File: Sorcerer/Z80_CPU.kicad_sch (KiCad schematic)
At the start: 8 parts, among them U1 74LS241, U3 Z80CPU

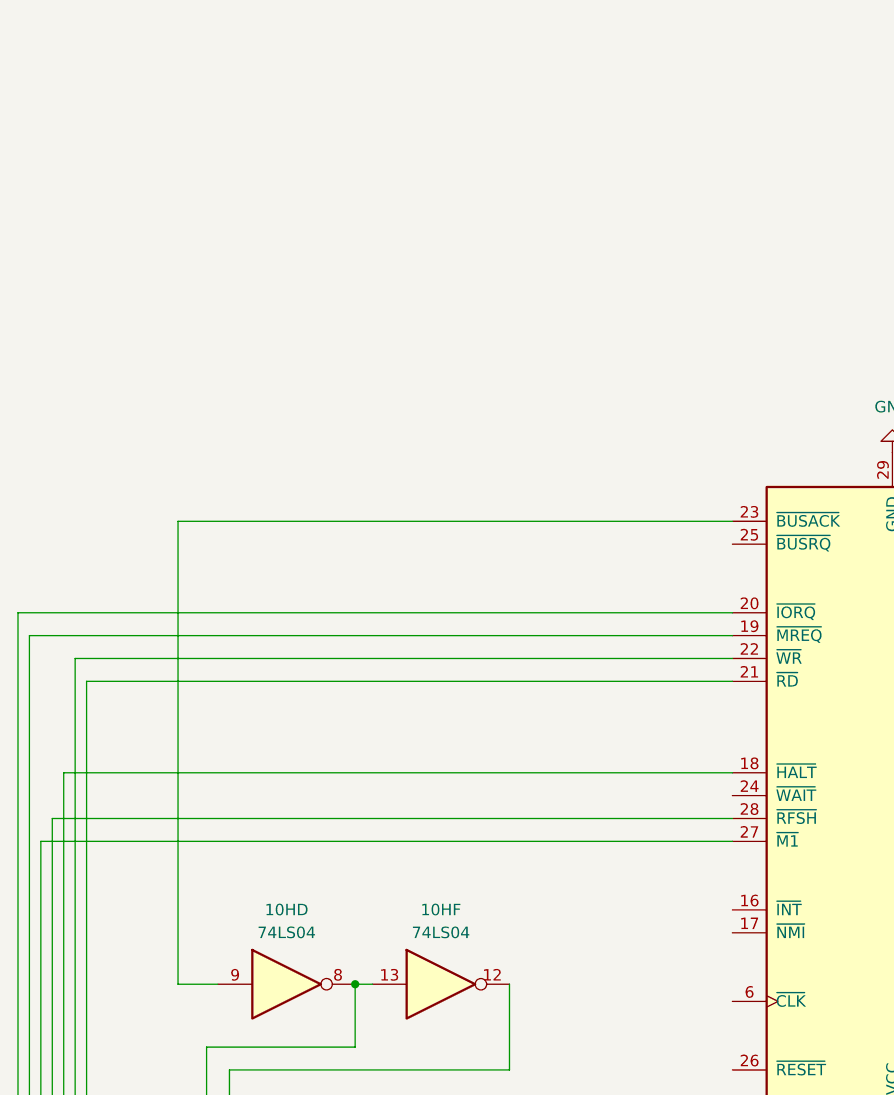
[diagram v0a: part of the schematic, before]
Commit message: More external symbols
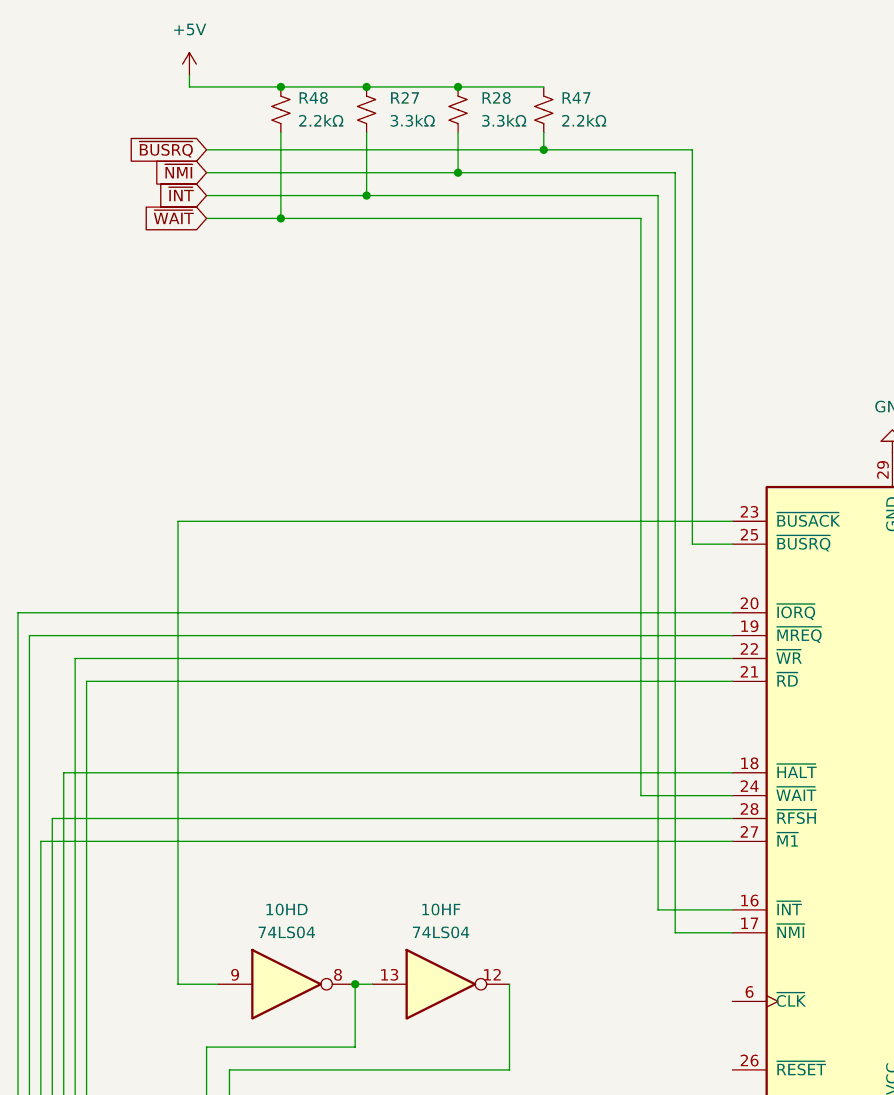
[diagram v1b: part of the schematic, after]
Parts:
- added R27, R28: 3.3kΩ, symbol Device:R_Small_US
- added R47, R48: 2.2kΩ, symbol Device:R_Small_US
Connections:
- net +5V: now also R27.1, R28.1, R47.1, R48.1
- net ~{INT}: now reaches U3.16 (~{INT})
- net ~{INT}: now also R27.2
- net ~{NMI}: now reaches U3.17 (~{NMI})
- net ~{NMI}: now also R28.2
- net ~{WAIT}: now reaches U3.24 (~{WAIT})
- net ~{WAIT}: now also R48.2
- net ~{BUSRQ}: now reaches U3.25 (~{BUSRQ})
- net ~{BUSRQ}: now also R47.2

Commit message: Clock generation
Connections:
- net ~{RESET}: now also U3.26 (~{RESET})
- net ~{BUSACK}: now reaches 10H.12, 6E.19 (OEb), 6F.19 (OEb), U1.19 (OEb)
- net Z80_Clock: now reaches U3.6 (~{CLK})
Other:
- added sheet Clock-Reset (Z80_Clock_Reset.kicad_sch)
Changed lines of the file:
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@@
 	)
 	(junction
+		(at 74.295 128.27)
+		(diameter 0)
+		(color 0 0 0 0)
+	)
+	(junction
 		(at 40.64 176.53)
 		(diameter 0)
@@
 	(wire
 		(pts
+			(xy 97.155 146.685) (xy 74.295 146.685)
+		)
+		(stroke
+			(width 0)
+			(type default)
+		)
+	)
+	(wire
+		(pts
 			(xy 92.71 113.03) (xy 92.71 28.575)
 		)
@@
 	(wire
 		(pts
+			(xy 83.185 120.65) (xy 99.06 120.65)
+		)
+		(stroke
+			(width 0)
+			(type default)
+		)
+	)
+	(wire
+		(pts
 			(xy 113.665 161.29) (xy 114.935 161.29)
 		)
@@
 	(wire
 		(pts
+			(xy 81.28 49.53) (xy 81.28 128.27)
+		)
+		(stroke
+			(width 0)
+			(type default)
+		)
+	)
+	(wire
+		(pts
 			(xy 180.34 118.11) (xy 134.62 118.11)
 		)
@@
 	(wire
 		(pts
+			(xy 74.295 146.685) (xy 74.295 128.27)
+		)
+		(stroke
+			(width 0)
+			(type default)
+		)
+	)
+	(wire
+		(pts
 			(xy 220.345 140.97) (xy 233.045 140.97)
 		)
@@
 	(wire
 		(pts
+			(xy 53.975 46.355) (xy 83.185 46.355)
+		)
+		(stroke
+			(width 0)
+			(type default)
+		)
+	)
+	(wire
+		(pts
 			(xy 177.8 146.05) (xy 177.8 128.27)
 		)
@@
 	(wire
 		(pts
+			(xy 81.28 128.27) (xy 99.06 128.27)
+		)
+		(stroke
+			(width 0)
+			(type default)
+		)
+	)
+	(wire
+		(pts
 			(xy 179.07 81.915) (xy 194.945 81.915)
 		)
@@
 	(wire
 		(pts
+			(xy 53.975 49.53) (xy 81.28 49.53)
+		)
+		(stroke
+			(width 0)
+			(type default)
+		)
+	)
+	(wire
+		(pts
 			(xy 179.07 81.915) (xy 179.07 92.71)
 		)
@@
 	(wire
 		(pts
+			(xy 83.185 46.355) (xy 83.185 120.65)
+		)
+		(stroke
+			(width 0)
+			(type default)
+		)
+	)
+	(wire
+		(pts
 			(xy 180.975 89.535) (xy 194.945 89.535)
 		)
@@
 		)
 	)
+	(global_label "Z80_Clock"
+		(shape input)
+		(at 53.975 46.355 180)
+		(fields_autoplaced yes)
+		(effects
+			(font
+				(size 1.27 1.27)
+			)
+			(justify right)
+		)
+		(property "Intersheetrefs" "${INTERSHEET_REFS}"
+			(at 41.1928 46.355 0)
+			(effects
+				(font
+					(size 1.27 1.27)
+				)
+				(justify right)
+				(hide yes)
+			)
+		)
+	)
 	(global_label "~{NMI}"
 		(shape input)
@@
 		)
 	)
+	(global_label "~{BUSACK}"
+		(shape input)
+		(at 97.155 146.685 0)
+		(fields_autoplaced yes)
+		(effects
+			(font
+				(size 1.27 1.27)
+			)
+			(justify left)
+		)
+		(property "Intersheetrefs" "${INTERSHEET_REFS}"
+			(at 107.5788 146.685 0)
+			(effects
+				(font
+					(size 1.27 1.27)
+				)
+				(justify left)
+				(hide yes)
+			)
+		)
+	)
 	(global_label "D2"
 		(shape input)
@@
 		)
 	)
-	(global_label "~{RESET}"
-		(shape input)
-		(at 233.68 21.59 0)
-		(fields_autoplaced yes)
-		(effects
-			(font
-				(size 1.27 1.27)
-			)
-			(justify left)
-		)
-		(property "Intersheetrefs" "${INTERSHEET_REFS}"
-			(at 242.4103 21.59 0)
-			(effects
-				(font
-					(size 1.27 1.27)
-				)
-				(justify left)
-				(hide yes)
-			)
-		)
-	)
 	(global_label "A2"
 		(shape input)
@@
 		)
 	)
+	(global_label "~{RESET}"
+		(shape input)
+		(at 53.975 49.53 180)
+		(fields_autoplaced yes)
+		(effects
+			(font
+				(size 1.27 1.27)
+			)
+			(justify right)
+		)
+		(property "Intersheetrefs" "${INTERSHEET_REFS}"
+			(at 45.2447 49.53 0)
+			(effects
+				(font
+					(size 1.27 1.27)
+				)
+				(justify right)
+				(hide yes)
+			)
+		)
+	)
 	(global_label "D3"
 		(shape input)
@@
 				)
 			)
+		)
+	)
+	(sheet
+		(at 25.4 45.085)
+		(size 12.7 9.525)
+		(exclude_from_sim no)
+		(in_bom yes)
+		(on_board yes)
+		(dnp no)
+		(fields_autoplaced yes)
+		(stroke
+			(width 0.1524)
+			(type solid)
+		)
+		(fill
+			(color 0 0 0 0.0000)
+		)
+		(property "Sheetname" "Clock-Reset"
+			(at 25.4 44.3734 0)
+			(effects
+				(font
+					(size 1.27 1.27)
+				)
+				(justify left bottom)
+			)
+		)
+		(property "Sheetfile" "Z80_Clock_Reset.kicad_sch"
+			(at 25.4 55.1946 0)
+			(effects
+				(font
+					(size 1.27 1.27)
+				)
+				(justify left top)
+			)
+		)
+		(instances
+			(project "Sorcerer"
+				(path "/a206b757-c4ba-4c88-b029-4cf0643816b3/9f27243c-e3ff-46f7-9a7c-c428f4adfc65"
+					(page "3")
+				)
+			)
